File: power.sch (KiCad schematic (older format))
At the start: 18 parts

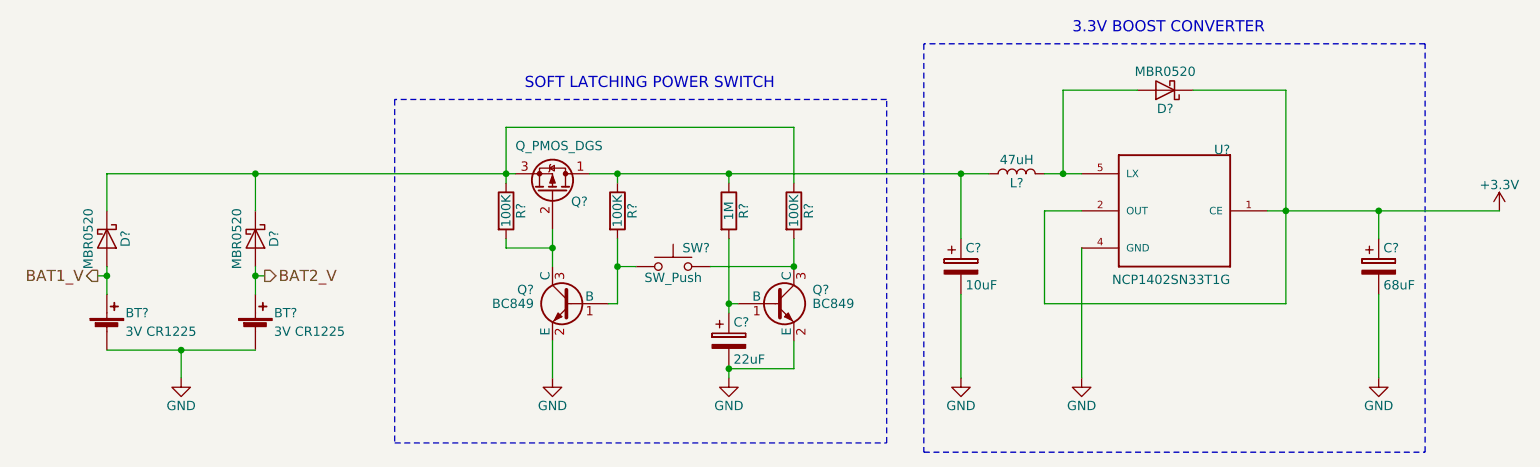
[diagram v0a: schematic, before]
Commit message: Make top-level connections between microcontroller and everything else
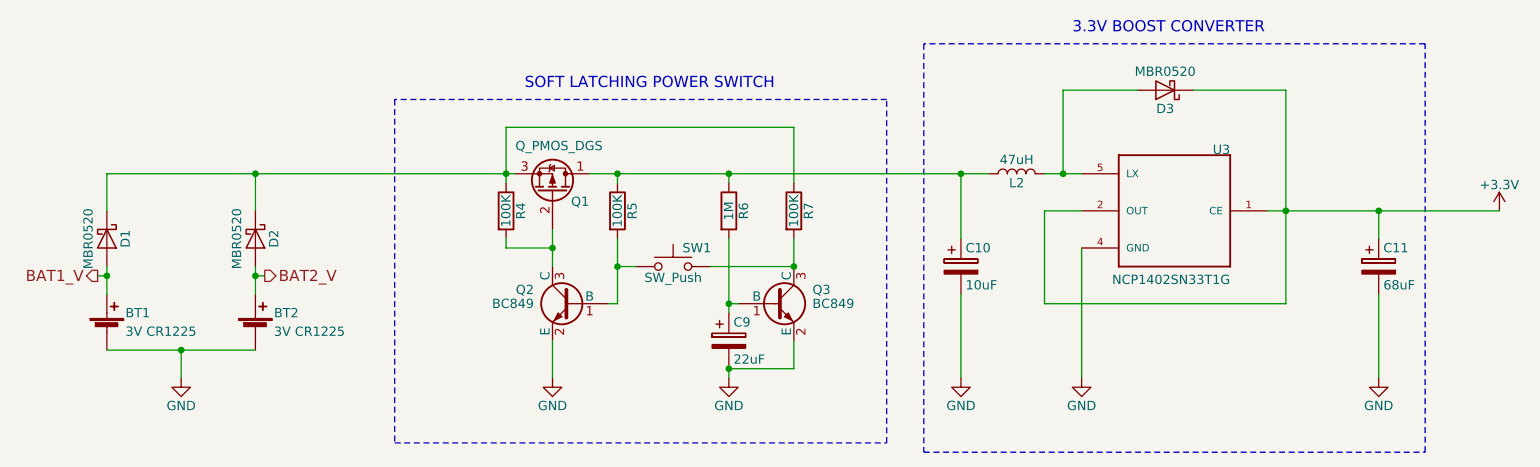
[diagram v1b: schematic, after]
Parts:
- U3: renamed from U?; footprint SOT95P275X110-5N -> (none)
- gave numbers to parts that had none: 17
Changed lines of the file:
@@
 $EndDescr
 $Comp
-L Battery_Cell BT?
+L Battery_Cell BT1
 U 1 1 59A122C7
 P 1500 4050
-F 0 "BT?" H 1600 4150 50  0000 L CNN
+F 0 "BT1" H 1600 4150 50  0000 L CNN
 F 1 "3V CR1225" H 1600 4050 50  0000 L CNN
 F 2 "" V 1500 4110 50  0001 C CNN
@@
 $EndComp
 $Comp
-L Battery_Cell BT?
+L Battery_Cell BT2
 U 1 1 59A123DB
 P 2300 4050
-F 0 "BT?" H 2400 4150 50  0000 L CNN
+F 0 "BT2" H 2400 4150 50  0000 L CNN
 F 1 "3V CR1225" H 2400 4050 50  0000 L CNN
 F 2 "" V 2300 4110 50  0001 C CNN
@@
 	1500 4150 2300 4150
 $Comp
-L GND #PWR?
+L GND #PWR014
 U 1 1 59A124B6
 P 1900 4300
-F 0 "#PWR?" H 1900 4050 50  0001 C CNN
+F 0 "#PWR014" H 1900 4050 50  0001 C CNN
 F 1 "GND" H 1900 4150 50  0000 C CNN
 F 2 "" H 1900 4300 50  0001 C CNN
@@
 	1500 3200 1500 3400
 $Comp
-L Q_PMOS_DGS Q?
+L Q_PMOS_DGS Q1
 U 1 1 59A1327C
 P 3900 3300
-F 0 "Q?" V 3850 3400 50  0000 L CNN
+F 0 "Q1" V 3850 3400 50  0000 L CNN
 F 1 "Q_PMOS_DGS" V 4150 3100 50  0000 L CNN
 F 2 "" H 4100 3400 50  0001 C CNN
@@
 $EndComp
 $Comp
-L R R?
+L R R4
 U 1 1 59A13323
 P 3650 3400
-F 0 "R?" V 3730 3400 50  0000 C CNN
+F 0 "R4" V 3730 3400 50  0000 C CNN
 F 1 "100K" V 3650 3400 50  0000 C CNN
 F 2 "" V 3580 3400 50  0001 C CNN
@@
 $EndComp
 $Comp
-L BC849 Q?
+L BC849 Q2
 U 1 1 59A133DB
 P 4000 3900
-F 0 "Q?" H 4200 3975 50  0000 L CNN
+F 0 "Q2" H 4200 3975 50  0000 L CNN
 F 1 "BC849" H 4200 3900 50  0000 L CNN
 F 2 "TO_SOT_Packages_SMD:SOT-23" H 4200 3825 50  0001 L CIN
@@
 Connection ~ 3650 3200
 $Comp
-L R R?
+L R R5
 U 1 1 59A13496
 P 4250 3400
-F 0 "R?" V 4330 3400 50  0000 C CNN
+F 0 "R5" V 4330 3400 50  0000 C CNN
 F 1 "100K" V 4250 3400 50  0000 C CNN
 F 2 "" V 4180 3400 50  0001 C CNN
@@
 	3900 4100 3900 4300
 $Comp
-L GND #PWR?
+L GND #PWR015
 U 1 1 59A13534
 P 3900 4300
-F 0 "#PWR?" H 3900 4050 50  0001 C CNN
+F 0 "#PWR015" H 3900 4050 50  0001 C CNN
 F 1 "GND" H 3900 4150 50  0000 C CNN
 F 2 "" H 3900 4300 50  0001 C CNN
@@
 $EndComp
 $Comp
-L R R?
+L R R6
 U 1 1 59A13557
 P 4850 3400
-F 0 "R?" V 4930 3400 50  0000 C CNN
+F 0 "R6" V 4930 3400 50  0000 C CNN
 F 1 "1M" V 4850 3400 50  0000 C CNN
 F 2 "" V 4780 3400 50  0001 C CNN
@@
 $EndComp
 $Comp
-L SW_Push SW?
+L SW_Push SW1
 U 1 1 59A13615
 P 4550 3700
-F 0 "SW?" H 4600 3800 50  0000 L CNN
+F 0 "SW1" H 4600 3800 50  0000 L CNN
 F 1 "SW_Push" H 4550 3640 50  0000 C CNN
 F 2 "" H 4550 3900 50  0001 C CNN
@@
 $EndComp
 $Comp
-L BC849 Q?
+L BC849 Q3
 U 1 1 59A1366E
 P 5100 3900
-F 0 "Q?" H 5300 3975 50  0000 L CNN
+F 0 "Q3" H 5300 3975 50  0000 L CNN
 F 1 "BC849" H 5300 3900 50  0000 L CNN
 F 2 "TO_SOT_Packages_SMD:SOT-23" H 5300 3825 50  0001 L CIN
@@
 	4850 3900 4900 3900
 $Comp
-L CP C?
+L CP C9
 U 1 1 59A13775
 P 4850 4100
-F 0 "C?" H 4875 4200 50  0000 L CNN
+F 0 "C9" H 4875 4200 50  0000 L CNN
 F 1 "22uF" H 4875 4000 50  0000 L CNN
 F 2 "" H 4888 3950 50  0001 C CNN
@@
 $EndComp
 $Comp
-L GND #PWR?
+L GND #PWR016
 U 1 1 59A13838
 P 4850 4300
-F 0 "#PWR?" H 4850 4050 50  0001 C CNN
+F 0 "#PWR016" H 4850 4050 50  0001 C CNN
 F 1 "GND" H 4850 4150 50  0000 C CNN
 F 2 "" H 4850 4300 50  0001 C CNN
@@
 Connection ~ 4250 3200
 $Comp
-L R R?
+L R R7
 U 1 1 59A13DCA
 P 5200 3400
-F 0 "R?" V 5280 3400 50  0000 C CNN
+F 0 "R7" V 5280 3400 50  0000 C CNN
 F 1 "100K" V 5200 3400 50  0000 C CNN
 F 2 "" V 5130 3400 50  0001 C CNN
@@
 SOFT LATCHING POWER SWITCH
 $Comp
-L NCP1402SN33T1G U?
+L NCP1402SN33T1G U3
 U 1 1 59A162C7
 P 7250 3400
-F 0 "U?" H 6950 3700 50  0000 L BNN
+F 0 "U3" H 6950 3700 50  0000 L BNN
 F 1 "NCP1402SN33T1G" H 6950 3000 50  0000 L BNN
-F 2 "SOT95P275X110-5N" H 7250 3400 50  0001 L BNN
+F 2 "" H 7250 3400 50  0001 L BNN
 F 3 "None" H 7250 3400 50  0001 L BNN
 F 4 "Unavailable" H 7250 3400 50  0001 L BNN "Availability"
@@
 	7750 3400 9000 3400
 $Comp
-L L L?
+L L L2
 U 1 1 59A16AB1
 P 6400 3200
-F 0 "L?" V 6350 3200 50  0000 C CNN
+F 0 "L2" V 6350 3200 50  0000 C CNN
 F 1 "47uH" V 6475 3200 50  0000 C CNN
 F 2 "" H 6400 3200 50  0001 C CNN
@@
 	6550 3200 6750 3200
 $Comp
-L CP C?
+L CP C10
 U 1 1 59A171A3
 P 6100 3700
-F 0 "C?" H 6125 3800 50  0000 L CNN
+F 0 "C10" H 6125 3800 50  0000 L CNN
 F 1 "10uF" H 6125 3600 50  0000 L CNN
 F 2 "" H 6138 3550 50  0001 C CNN
@@
 $EndComp
 $Comp
-L CP C?
+L CP C11
 U 1 1 59A174A2
 P 8350 3700
-F 0 "C?" H 8375 3800 50  0000 L CNN
+F 0 "C11" H 8375 3800 50  0000 L CNN
 F 1 "68uF" H 8375 3600 50  0000 L CNN
 F 2 "" H 8388 3550 50  0001 C CNN
@@
 	8350 3850 8350 4300
 $Comp
-L MBR0520 D?
+L MBR0520 D3
 U 1 1 59A1778B
 P 7200 2750
-F 0 "D?" H 7200 2850 50  0000 C CNN
+F 0 "D3" H 7200 2850 50  0000 C CNN
 F 1 "MBR0520" H 7200 2650 50  0000 C CNN
 F 2 "Diodes_SMD:SOD-123" H 7200 2575 50  0001 C CNN
@@
 	7850 2750 7350 2750
 $Comp
-L MBR0520 D?
+L MBR0520 D1
 U 1 1 59A17EC1
 P 1500 3550
-F 0 "D?" H 1500 3650 50  0000 C CNN
+F 0 "D1" H 1500 3650 50  0000 C CNN
 F 1 "MBR0520" H 1500 3450 50  0000 C CNN
 F 2 "Diodes_SMD:SOD-123" H 1500 3375 50  0001 C CNN
@@
 $EndComp
 $Comp
-L MBR0520 D?
+L MBR0520 D2
 U 1 1 59A17F48
 P 2300 3550
-F 0 "D?" H 2300 3650 50  0000 C CNN
+F 0 "D2" H 2300 3650 50  0000 C CNN
 F 1 "MBR0520" H 2300 3450 50  0000 C CNN
 F 2 "Diodes_SMD:SOD-123" H 2300 3375 50  0001 C CNN
@@
 $EndComp
 $Comp
-L GND #PWR?
+L GND #PWR017
 U 1 1 59A1839A
 P 6100 4300
-F 0 "#PWR?" H 6100 4050 50  0001 C CNN
+F 0 "#PWR017" H 6100 4050 50  0001 C CNN
 F 1 "GND" H 6100 4150 50  0000 C CNN
 F 2 "" H 6100 4300 50  0001 C CNN
@@
 $EndComp
 $Comp
-L GND #PWR?
+L GND #PWR018
 U 1 1 59A183DB
 P 6750 4300
-F 0 "#PWR?" H 6750 4050 50  0001 C CNN
+F 0 "#PWR018" H 6750 4050 50  0001 C CNN
 F 1 "GND" H 6750 4150 50  0000 C CNN
 F 2 "" H 6750 4300 50  0001 C CNN
@@
 $EndComp
 $Comp
-L GND #PWR?
+L GND #PWR019
 U 1 1 59A1841C
 P 8350 4300
-F 0 "#PWR?" H 8350 4050 50  0001 C CNN
+F 0 "#PWR019" H 8350 4050 50  0001 C CNN
 F 1 "GND" H 8350 4150 50  0000 C CNN
 F 2 "" H 8350 4300 50  0001 C CNN
@@
 Connection ~ 8350 3400
 $Comp
-L +3.3V #PWR?
+L +3.3V #PWR020
 U 1 1 59A19F08
 P 9000 3400
-F 0 "#PWR?" H 9000 3250 50  0001 C CNN
+F 0 "#PWR020" H 9000 3250 50  0001 C CNN
 F 1 "+3.3V" H 9000 3540 50  0000 C CNN
 F 2 "" H 9000 3400 50  0001 C CNN

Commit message: Assigned some footprints and added CR1225 holder footprint
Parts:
- BT1, BT2: footprint (none) -> BC_2011_CR1225_HOLDER:BC-2011-CR1225
- C10, C11, C9: footprint (none) -> Capacitors_Tantalum_SMD:CP_Tantalum_Case-B_EIA-3528-21_Reflow
- R4, R5, R6, R7: footprint (none) -> Resistors_SMD:R_0603
- U3: footprint (none) -> NCP1402SN33T1G:SOT95P275X110-5N
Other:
- note added: "(BC-2011 Holder)"
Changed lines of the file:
@@
 F 0 "BT1" H 1600 4150 50  0000 L CNN
 F 1 "3V CR1225" H 1600 4050 50  0000 L CNN
-F 2 "" V 1500 4110 50  0001 C CNN
+F 2 "BC_2011_CR1225_HOLDER:BC-2011-CR1225" V 1500 4110 50  0001 C CNN
 F 3 "" V 1500 4110 50  0001 C CNN
 	1    1500 4050
@@
 F 0 "BT2" H 2400 4150 50  0000 L CNN
 F 1 "3V CR1225" H 2400 4050 50  0000 L CNN
-F 2 "" V 2300 4110 50  0001 C CNN
+F 2 "BC_2011_CR1225_HOLDER:BC-2011-CR1225" V 2300 4110 50  0001 C CNN
 F 3 "" V 2300 4110 50  0001 C CNN
 	1    2300 4050
@@
 F 0 "R4" V 3730 3400 50  0000 C CNN
 F 1 "100K" V 3650 3400 50  0000 C CNN
-F 2 "" V 3580 3400 50  0001 C CNN
+F 2 "Resistors_SMD:R_0603" V 3580 3400 50  0001 C CNN
 F 3 "" H 3650 3400 50  0001 C CNN
 	1    3650 3400
@@
 F 0 "R5" V 4330 3400 50  0000 C CNN
 F 1 "100K" V 4250 3400 50  0000 C CNN
-F 2 "" V 4180 3400 50  0001 C CNN
+F 2 "Resistors_SMD:R_0603" V 4180 3400 50  0001 C CNN
 F 3 "" H 4250 3400 50  0001 C CNN
 	1    4250 3400
@@
 F 0 "R6" V 4930 3400 50  0000 C CNN
 F 1 "1M" V 4850 3400 50  0000 C CNN
-F 2 "" V 4780 3400 50  0001 C CNN
+F 2 "Resistors_SMD:R_0603" V 4780 3400 50  0001 C CNN
 F 3 "" H 4850 3400 50  0001 C CNN
 	1    4850 3400
@@
 F 0 "C9" H 4875 4200 50  0000 L CNN
 F 1 "22uF" H 4875 4000 50  0000 L CNN
-F 2 "" H 4888 3950 50  0001 C CNN
+F 2 "Capacitors_Tantalum_SMD:CP_Tantalum_Case-B_EIA-3528-21_Reflow" H 4888 3950 50  0001 C CNN
 F 3 "" H 4850 4100 50  0001 C CNN
 	1    4850 4100
@@
 F 0 "R7" V 5280 3400 50  0000 C CNN
 F 1 "100K" V 5200 3400 50  0000 C CNN
-F 2 "" V 5130 3400 50  0001 C CNN
+F 2 "Resistors_SMD:R_0603" V 5130 3400 50  0001 C CNN
 F 3 "" H 5200 3400 50  0001 C CNN
 	1    5200 3400
@@
 F 0 "U3" H 6950 3700 50  0000 L BNN
 F 1 "NCP1402SN33T1G" H 6950 3000 50  0000 L BNN
-F 2 "" H 7250 3400 50  0001 L BNN
+F 2 "NCP1402SN33T1G:SOT95P275X110-5N" H 7250 3400 50  0001 L BNN
 F 3 "None" H 7250 3400 50  0001 L BNN
 F 4 "Unavailable" H 7250 3400 50  0001 L BNN "Availability"
@@
 F 0 "C10" H 6125 3800 50  0000 L CNN
 F 1 "10uF" H 6125 3600 50  0000 L CNN
-F 2 "" H 6138 3550 50  0001 C CNN
+F 2 "Capacitors_Tantalum_SMD:CP_Tantalum_Case-B_EIA-3528-21_Reflow" H 6138 3550 50  0001 C CNN
 F 3 "" H 6100 3700 50  0001 C CNN
 	1    6100 3700
@@
 F 0 "C11" H 8375 3800 50  0000 L CNN
 F 1 "68uF" H 8375 3600 50  0000 L CNN
-F 2 "" H 8388 3550 50  0001 C CNN
+F 2 "Capacitors_Tantalum_SMD:CP_Tantalum_Case-B_EIA-3528-21_Reflow" H 8388 3550 50  0001 C CNN
 F 3 "" H 8350 3700 50  0001 C CNN
 	1    8350 3700
@@
 Text HLabel 2350 3750 2    60   Output ~ 0
 BAT2_V
+Text Notes 2100 4350 0    60   ~ 0
+(BC-2011 Holder)
 $EndSCHEMATC

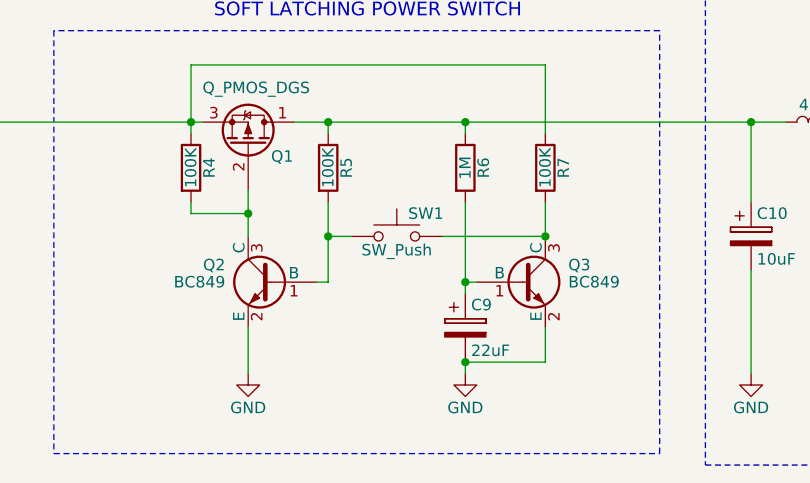
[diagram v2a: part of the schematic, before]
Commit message: Add switch footprints, add mode switch
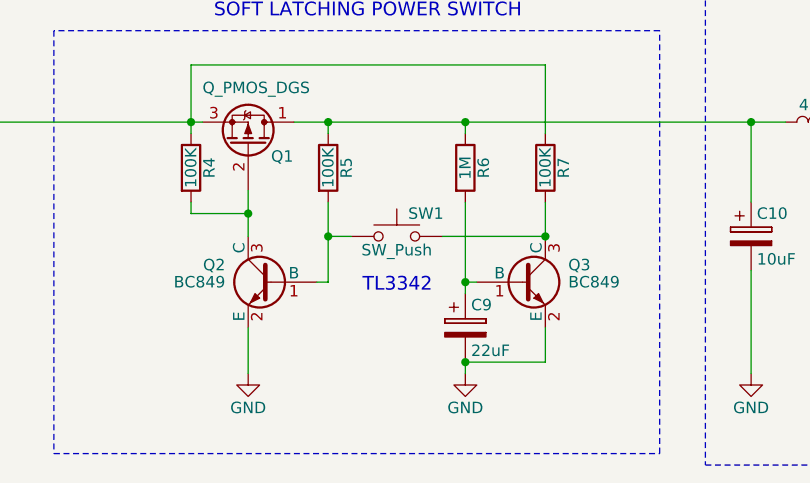
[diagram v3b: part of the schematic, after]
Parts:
- L2: footprint (none) -> Inductors_SMD:L_0603
- Q1: footprint (none) -> TO_SOT_Packages_SMD:SOT-23
- SW1: footprint (none) -> Buttons_Switches_SMD:SW_SPST_TL3342
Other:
- note added: "TL3342"
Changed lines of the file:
@@
 F 0 "Q1" V 3850 3400 50  0000 L CNN
 F 1 "Q_PMOS_DGS" V 4150 3100 50  0000 L CNN
-F 2 "" H 4100 3400 50  0001 C CNN
+F 2 "TO_SOT_Packages_SMD:SOT-23" H 4100 3400 50  0001 C CNN
 F 3 "" H 3900 3300 50  0001 C CNN
 	1    3900 3300
@@
 F 0 "SW1" H 4600 3800 50  0000 L CNN
 F 1 "SW_Push" H 4550 3640 50  0000 C CNN
-F 2 "" H 4550 3900 50  0001 C CNN
+F 2 "Buttons_Switches_SMD:SW_SPST_TL3342" H 4550 3900 50  0001 C CNN
 F 3 "" H 4550 3900 50  0001 C CNN
 	1    4550 3700
@@
 F 0 "L2" V 6350 3200 50  0000 C CNN
 F 1 "47uH" V 6475 3200 50  0000 C CNN
-F 2 "" H 6400 3200 50  0001 C CNN
+F 2 "Inductors_SMD:L_0603" H 6400 3200 50  0001 C CNN
 F 3 "" H 6400 3200 50  0001 C CNN
 	1    6400 3200
@@
 Text Notes 2100 4350 0    60   ~ 0
 (BC-2011 Holder)
+Text Notes 4400 3950 0    60   ~ 0
+TL3342
 $EndSCHEMATC

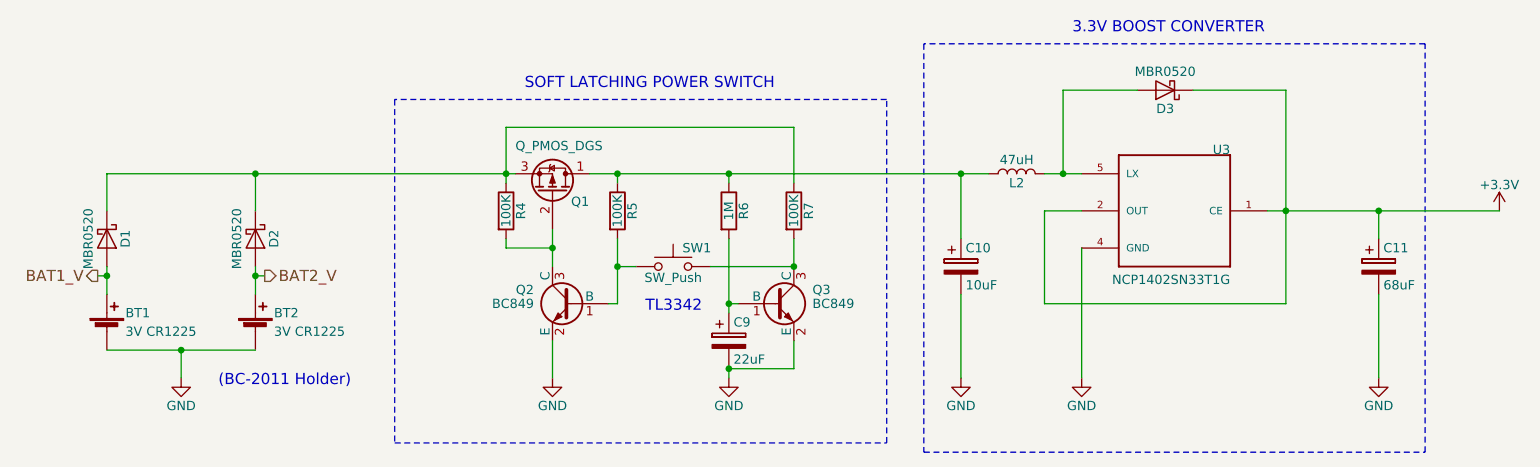
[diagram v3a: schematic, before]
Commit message: Update to new soft-latching power circuit
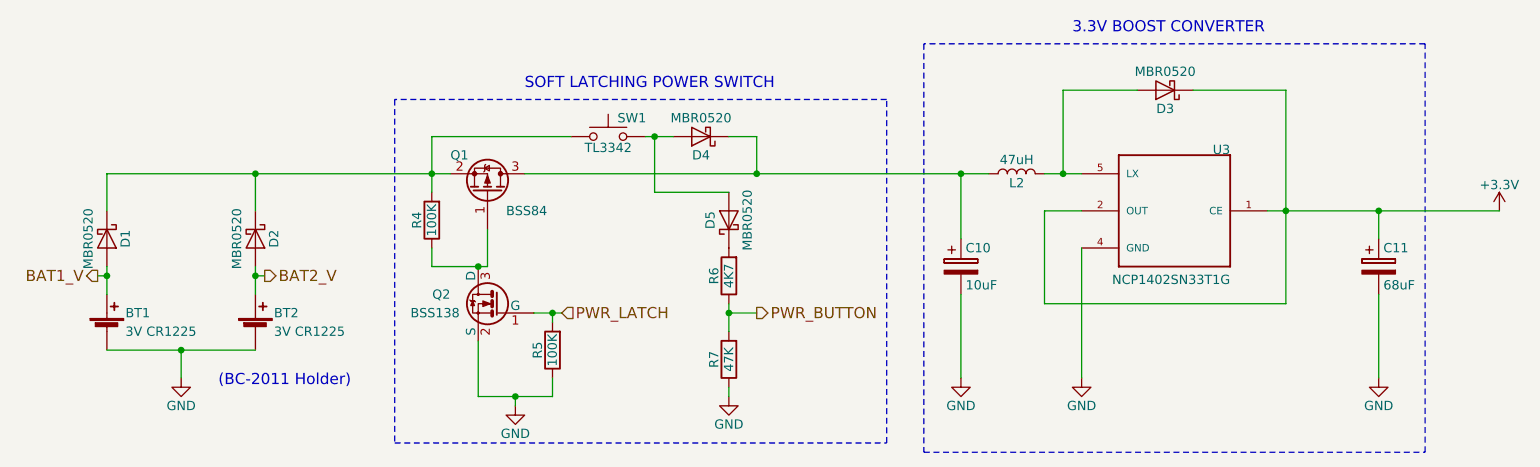
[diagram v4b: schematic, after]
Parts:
- removed C9: 22uF, Capacitors_Tantalum_SMD:CP_Tantalum_Case-B_EIA-3528-21_Reflow, symbol CP
- removed Q1: Q_PMOS_DGS, TO_SOT_Packages_SMD:SOT-23, symbol Q_PMOS_DGS
- removed Q2, Q3: BC849, TO_SOT_Packages_SMD:SOT-23, symbol BC849
- added D4, D5: MBR0520, Diodes_SMD:D_SOD-123, symbol MBR0520
- added Q1: BSS84, TO_SOT_Packages_SMD:SOT-23, symbol Q_PMOS_GSD
- added Q2: BSS138, TO_SOT_Packages_SMD:SOT-23, symbol BSS138
- D1, D2, D3: footprint Diodes_SMD:SOD-123 -> Diodes_SMD:D_SOD-123
- R6: value 1M -> 4K7
- R7: value 100K -> 47K
- SW1: value SW_Push -> TL3342
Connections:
- net GND: now also R5.1, R7.1, Q2.2 (S)
- net at C10.1, L2.1: now also D4.1 (K), Q1.3 (D); no longer R5.1, R6.1
- net at R4.2: now also D1.1 (K), D2.1 (K), SW1.1, Q1.2 (S)
- net PWR_LATCH: now reaches R5.2
- net PWR_LATCH: now also Q2.1 (G); no longer SW1.1
- net at R6.2: now also D5.1 (K)
- net at SW1.2: now also D4.2 (A), D5.2 (A); no longer R7.2
- new net: Q1.1 (G), Q2.3 (D), R4.1
- new net PWR_BUTTON: R6.1, R7.2
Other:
- note removed: "TL3342"
- moved on the sheet: SW1

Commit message: attempt 1
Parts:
- removed BT2: 3V CR1225, BC_2011_CR1225_HOLDER:BC-2011-CR1225, symbol Battery_Cell
- removed D2: MBR0520, Diodes_SMD:D_SOD-123, symbol MBR0520
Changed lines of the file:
@@
-	1    0    0    -1
-$EndComp
-$Comp
-L Battery_Cell BT2
-U 1 1 59A123DB
-P 2300 4050
-F 0 "BT2" H 2400 4150 50  0000 L CNN
-F 1 "3V CR1225" H 2400 4050 50  0000 L CNN
-F 2 "BC_2011_CR1225_HOLDER:BC-2011-CR1225" V 2300 4110 50  0001 C CNN
-F 3 "" V 2300 4110 50  0001 C CNN
-	1    2300 4050
 	1    0    0    -1
 $EndComp
 Wire Wire Line
 	1500 3700 1500 3850
-Wire Wire Line
-	2300 3850 2300 3700
-Wire Wire Line
-	1500 4150 2300 4150
 $Comp
 L GND #PWR014
 U 1 1 59A124B6
-P 1900 4300
-F 0 "#PWR014" H 1900 4050 50  0001 C CNN
-F 1 "GND" H 1900 4150 50  0000 C CNN
-F 2 "" H 1900 4300 50  0001 C CNN
-F 3 "" H 1900 4300 50  0001 C CNN
-	1    1900 4300
-	1    0    0    -1
-$EndComp
-Wire Wire Line
-	1900 4150 1900 4300
-Connection ~ 1900 4150
-Wire Wire Line
-	2300 3400 2300 3200
+P 1500 4300
+F 0 "#PWR014" H 1500 4050 50  0001 C CNN
+F 1 "GND" H 1500 4150 50  0000 C CNN
+F 2 "" H 1500 4300 50  0001 C CNN
+F 3 "" H 1500 4300 50  0001 C CNN
+	1    1500 4300
+	1    0    0    -1
+$EndComp
+Wire Wire Line
+	1500 4150 1500 4300
 Wire Wire Line
 	1500 3200 1500 3400
-Connection ~ 2300 3200
 $Comp
 L SW_Push SW1
@@
 $EndComp
 $Comp
-L MBR0520 D2
-U 1 1 59A17F48
-P 2300 3550
-F 0 "D2" H 2300 3650 50  0000 C CNN
-F 1 "MBR0520" H 2300 3450 50  0000 C CNN
-F 2 "Diodes_SMD:D_SOD-123" H 2300 3375 50  0001 C CNN
-F 3 "" H 2300 3550 50  0001 C CNN
-	1    2300 3550
-	0    1    1    0
-$EndComp
-$Comp
 L GND #PWR015
 U 1 1 59A1839A
@@
 $EndComp
 Wire Wire Line
-	2300 3750 2350 3750
-Connection ~ 2300 3750
-Wire Wire Line
 	1500 3750 1450 3750
 Connection ~ 1500 3750
 Text HLabel 1450 3750 0    60   Output ~ 0
 BAT1_V
-Text HLabel 2350 3750 2    60   Output ~ 0
-BAT2_V
-Text Notes 2100 4350 0    60   ~ 0
+Text Notes 1750 3750 0    60   ~ 0
 (BC-2011 Holder)
 Wire Wire Line

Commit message: More changes, replace
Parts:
- removed D1: MBR0520, Diodes_SMD:D_SOD-123, symbol MBR0520
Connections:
- net BAT1_V: now also Q1.2 (S), R4.2, SW1.1
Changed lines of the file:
@@
 $EndComp
 Wire Wire Line
-	1500 3700 1500 3850
+	1500 3200 1500 3850
 $Comp
 L GND #PWR014
@@
 Wire Wire Line
 	1500 4150 1500 4300
-Wire Wire Line
-	1500 3200 1500 3400
 $Comp
 L SW_Push SW1
@@
 	7850 2750 7350 2750
 $Comp
-L MBR0520 D1
-U 1 1 59A17EC1
-P 1500 3550
-F 0 "D1" H 1500 3650 50  0000 C CNN
-F 1 "MBR0520" H 1500 3450 50  0000 C CNN
-F 2 "Diodes_SMD:D_SOD-123" H 1500 3375 50  0001 C CNN
-F 3 "" H 1500 3550 50  0001 C CNN
-	1    1500 3550
-	0    1    1    0
-$EndComp
-$Comp
 L GND #PWR015

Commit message: Create relevant BOM links, export digikey BOM
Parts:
- BT1: MFR (none) -> MPD (Memory Protection Devices); MPN (none) -> BC-2011; SPN (none) -> BC-2011-ND; SPR (none) -> https://www.digikey.com.au/
- C10: MFR (none) -> Vishay Sprague; MPN (none) -> 293D106X9016B2TE3; SPN (none) -> 718-1124-1-ND; SPR (none) -> https://www.digikey.com.au/
- C11: MFR (none) -> AVX; MPN (none) -> F930J686MBA; SPN (none) -> 478-8190-1-ND; SPR (none) -> https://www.digikey.com.au/
- D3, D4, D5: MFR (none) -> Fairchild/ON; MPN (none) -> MBR0520L; SPN (none) -> MBR0520LCT-ND; SPR (none) -> https://www.digikey.com.au/
- L2: MFR (none) -> Taiyo Yuden; MPN (none) -> CBMF1608T470K; SPN (none) -> 587-1722-1-ND; SPR (none) -> https://www.digikey.com.au/
- Q1: MFR (none) -> Diodes Inc.; MPN (none) -> BSS84-7-F; SPN (none) -> BSS84-FDICT-ND; SPR (none) -> https://www.digikey.com.au/
- Q2: MFR (none) -> Fairchild/ON; MPN (none) -> BSS138L; SPN (none) -> BSS138LCT-ND; SPR (none) -> https://www.digikey.com.au/
- SW1: MFR (none) -> E-Switch; MPN (none) -> TL3342F160QG/TR; SPN (none) -> EG2531CT-ND; SPR (none) -> https://www.digikey.com.au/
- U3: MFR (none) -> ON Semiconductor; MPN (none) -> NCP1402SN33T1G; SPN (none) -> 802-3143; SPR (none) -> http://au.rs-online.com
